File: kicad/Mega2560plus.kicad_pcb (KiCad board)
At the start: 4 copper layers, 53.3 x 101.6 mm, 146 parts, among them J1 USB_C_Receptacle_USB2.0_14P, J10 TC2030, J11 Conn_02x18_Odd_Even, J12 Conn_01x10, J13 Conn_01x08, J14 Conn_01x08, J15 Conn_02x06_Counter_Clockwise, J2 USB_C_Receptacle_USB2.0_14P, J3 Micro_SD_Card_Det2, J4 2.1mm ID 5.5mm OD PJ-102AH, J5 Conn_01x04_MountingPin, J6 Conn_01x04_MountingPin, J7 Conn_01x08, J8 Conn_01x08, J9 Conn_01x08, Q1 DMP3013SFV, SW1 SW_SPST, SW2 SW_SPST, SW3 SW_SPST, U1 USBLC6-2SC6, U10 TLV75733PDBV, U11 TLV75733PDBV, U12 SCD41-D-R2, U13 BME680, U14 LSM6DSL, U15 DS3231M, U16 SN74LVC1T45DBV, U17 SN74LVC1T45DBV, U2 FT231XS, U3 USBLC6-2SC6, U4 ESP32-S3-WROOM-1U-N16R8, U5 USBLC6-4SC6, U6 W25Q128JVS, U7 ATmega2560-16A, U8 FM24C64C, U9 TPS62163DSG

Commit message: finish pcb
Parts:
- removed the R7 at (303.0, 143.8)
- removed the R8 at (303.0, 146.3)
- added G***: LOGO, logo:empire_mask, F.Cu at (100.0, 100.0)
- added G***: LOGO, logo:linuxpenguin_cu, F.Cu at (117.8, 119.5)
- added G***: LOGO, logo:empire_cu, F.Cu at (100.0, 100.0)
- added G***: LOGO, logo:linuxpenguin-mask, F.Cu at (117.8, 119.5)
- added Y1: 16MHz X322516MLB4SI, Crystal:Crystal_SMD_3225-4Pin_3.2x2.5mm, F.Cu at (84.4, 96.2)
- BT1: footprint Battery:BatteryHolder_Keystone_1060_1x2032 -> Battery:BatteryHolder_LINX_BAT-HLD-012-SMT; moved to B.Cu
- C1, C10, C14, C15, C16, C2, C28, C29, C3, C30, C31, C32, C36, C37, C4, C5, C6, C7, C8: footprint Capacitor_SMD:C_0603_1608Metric -> Capacitor_SMD:C_0402_1005Metric
- C11: renamed from C12; value 16pF -> 18pF; footprint Capacitor_SMD:C_0603_1608Metric -> Capacitor_SMD:C_0402_1005Metric
- C12: renamed from C13; value 16pF -> 18pF; footprint Capacitor_SMD:C_0603_1608Metric -> Capacitor_SMD:C_0402_1005Metric
- C13: renamed from C11; footprint Capacitor_SMD:C_0603_1608Metric -> Capacitor_SMD:C_0402_1005Metric
- C43, C44, C45, C46, C9: footprint Capacitor_SMD:C_0603_1608Metric -> Capacitor_SMD:C_0805_2012Metric; moved to B.Cu
- D10, D11, D12, D14, D15, D16, D18, D6, D7, D8: footprint LED_SMD:LED_Avago_PLCC4_3.2x2.8mm_CW -> LED_SMD:LED_0402_1005Metric
- D2, F2, JP1, U16, U17, U5: moved to B.Cu
- J2: value USB_C_Receptacle_USB2.0_14P -> Conn_02x02_Counter_Clockwise; footprint Connector_USB:USB_C_Receptacle_HRO_TYPE-C-31-M-12 -> Connector_PinSocket_2.54mm:PinSocket_2x02_P2.54mm_Vertical
- J5, J6: footprint Connector_JST:JST_SH_SM04B-SRSS-TB_1x04-1MP_P1.00mm_Horizontal -> Connector_JST:JST_SH_BM04B-SRSS-TB_1x04-1MP_P1.00mm_Vertical
- R1, R2, R3, R4, R5: footprint Resistor_SMD:R_0603_1608Metric -> Resistor_SMD:R_0402_1005Metric
- R14: renamed from R16; footprint Resistor_SMD:R_0603_1608Metric -> Resistor_SMD:R_0805_2012Metric; moved to B.Cu
- R18: renamed from R20; footprint Resistor_SMD:R_0603_1608Metric -> Resistor_SMD:R_0402_1005Metric
- R20: renamed from R22; footprint Resistor_SMD:R_0603_1608Metric -> Resistor_SMD:R_0402_1005Metric
- R22: renamed from R24; footprint Resistor_SMD:R_0603_1608Metric -> Resistor_SMD:R_0402_1005Metric
- R23: renamed from R25; footprint Resistor_SMD:R_0603_1608Metric -> Resistor_SMD:R_0402_1005Metric
- R24: renamed from R26; footprint Resistor_SMD:R_0603_1608Metric -> Resistor_SMD:R_0402_1005Metric
- R25: renamed from R27; footprint Resistor_SMD:R_0603_1608Metric -> Resistor_SMD:R_0402_1005Metric
- R26: renamed from R28; footprint Resistor_SMD:R_0603_1608Metric -> Resistor_SMD:R_0402_1005Metric
- R27: renamed from R29; footprint Resistor_SMD:R_0603_1608Metric -> Resistor_SMD:R_0402_1005Metric
- R28: renamed from R30; footprint Resistor_SMD:R_0603_1608Metric -> Resistor_SMD:R_0402_1005Metric
- R29: renamed from R31; footprint Resistor_SMD:R_0603_1608Metric -> Resistor_SMD:R_0402_1005Metric
- R30: renamed from R32; footprint Resistor_SMD:R_0603_1608Metric -> Resistor_SMD:R_0402_1005Metric
- R31: renamed from R33; footprint Resistor_SMD:R_0603_1608Metric -> Resistor_SMD:R_0402_1005Metric
- R6: value 5.1k -> 22; footprint Resistor_SMD:R_0603_1608Metric -> Resistor_SMD:R_0402_1005Metric
- R7: renamed from R9; footprint Resistor_SMD:R_0603_1608Metric -> Resistor_SMD:R_0402_1005Metric
- R8: renamed from R10; footprint Resistor_SMD:R_0603_1608Metric -> Resistor_SMD:R_0402_1005Metric
- R9: renamed from R11; footprint Resistor_SMD:R_0603_1608Metric -> Resistor_SMD:R_0402_1005Metric
- SW2, SW3: footprint Button_Switch_SMD:SW_SPST_PTS645Sx43SMTR92 -> Button_Switch_SMD:SW_SPST_TS-1088-xR020
- moved C46 249.6 mm to (81.3, 85.3), turned to -90 degrees
- moved C32 242.9 mm to (93.4, 73.4), turned to 180 degrees
- moved C45 242.3 mm to (88.3, 85.3), turned to -90 degrees
- moved C31 240.6 mm to (93.4, 78.8), turned to 180 degrees
- moved C8 235.6 mm to (79.4, 66.0), turned to 90 degrees
- moved C29 234.9 mm to (98.2, 77.9), turned to 90 degrees
- moved R20 233.9 mm to (101.2, 80.9)
- moved C7 233.7 mm to (80.5, 66.0), turned to 90 degrees
- moved C12 233.6 mm to (84.4, 93.2), turned to 180 degrees
- moved R7 232.2 mm to (86.1, 66.1)
- moved C11 232.0 mm to (84.4, 99.2)
- moved R14 230.8 mm to (92.4, 63.9)
- moved C30 229.8 mm to (104.2, 77.9), turned to 90 degrees
- moved C15 229.6 mm to (88.9, 96.6), turned to -90 degrees
- moved R6 229.2 mm to (86.1, 67.3)
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- renumbered R12 to R10, R13 to R11, R14 to R12, R15 to R13, R17 to R15, R18 to R16, R19 to R17, R21 to R19, R23 to R21
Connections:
- C3 pad 2: UART3.3V -> +5V
- F2 pad 1: Net-(F2-Pad1) -> Net-(J2-Pin_1)
- R6 pad 1: Net-(J2-CC2) -> Net-(R6-Pad1)
- R6 pad 2: GND -> ESP32_USB_D+
- U2 pad 3: UART3.3V -> +5V
- U3 pad 1: Net-(J2-D--PadA7) -> Net-(J2-Pin_4)
- U3 pad 3: Net-(J2-D+-PadA6) -> Net-(J2-Pin_3)
- U3 pad 4: Net-(R7-Pad1) (its old number) -> Net-(R6-Pad1)
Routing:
- net GND: track 0.00 -> 242.1 mm, vias 0 -> 48
- net +3.3VP: track 0.00 -> 223.6 mm, vias 0 -> 7
- net +5V: track 0.00 -> 223.2 mm, vias 0 -> 13
- net AVR_SCL: track 0.00 -> 189.5 mm, vias 0 -> 3
- net +3.3V: track 0.00 -> 167.1 mm, vias 0 -> 12
- net AVR_SDA: track 0.00 -> 161.2 mm, vias 0 -> 3
- net /ESP32/I2C1_SCL: track 0.00 -> 154.5 mm, vias 0 -> 8
- net /ESP32/I2C1_SDA: track 0.00 -> 152.5 mm, vias 0 -> 8
- net /ESP32/RTC_INT: track 0.00 -> 92.1 mm, vias 0 -> 2
- net AVR_RESET: track 0.00 -> 80.4 mm, vias 0 -> 4
- net PB1: track 0.00 -> 75.6 mm, vias 0 -> 3
- net PB2: track 0.00 -> 74.7 mm, vias 0 -> 2
- net PB0: track 0.00 -> 73.7 mm, vias 0 -> 1
- net PB3: track 0.00 -> 73.5 mm, vias 0 -> 2
- net ESP_RESET: track 0.00 -> 70.5 mm, vias 0 -> 3
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- added copper zone on In2.Cu, net +3.3V
- added copper zone on In2.Cu, net +3.3VP
- added copper zone on In2.Cu, net +5V
- added copper zone on In4.Cu, net GND
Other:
- copper layers 4 -> 6
- board text added: "3.3V"
- board text added: "5V"
- board text added: "Converts Bitcoins into Dreams."
- board text added: "Designed in Canada"
- board text added: "Keep Going!"
- board text added: "Mega 2560+"

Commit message: add spinning render
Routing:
- net ESP32_NPX: track 0.00 -> 63.3 mm, vias 0 -> 2
- net AVR_SDA: track 161.2 -> 144.5 mm, vias 3 -> 2
- net AVR_SCL: track 189.5 -> 173.0 mm, vias 3 -> 2
- net +5V: track 223.2 -> 227.2 mm, vias 13 -> 14
- net Net-(D18-A): track 0.00 -> 1.01 mm
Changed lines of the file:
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@@
 	)
 	(segment
+		(start 116.395 82.905)
+		(end 116.8 82.5)
+		(width 0.2)
+		(layer "F.Cu")
+		(net "+5V")
+	)
+	(segment
 		(start 107.9 65.49)
 		(end 107.385 65.49)
@@
 	)
 	(segment
+		(start 116.395 84.325)
+		(end 116.395 82.905)
+		(width 0.2)
+		(layer "F.Cu")
+		(net "+5V")
+	)
+	(segment
 		(start 82.275 87.475001)
 		(end 82.1 87.650001)
@@
 	)
 	(via
+		(at 116.8 82.5)
+		(size 0.6)
+		(drill 0.3)
+		(layers "F.Cu" "B.Cu")
+		(net "+5V")
+	)
+	(via
 		(at 117.925 128.3)
 		(size 0.6)
@@
 	)
 	(segment
+		(start 117 83.55)
+		(end 117.65 84.2)
+		(width 0.2)
+		(layer "B.Cu")
+		(net "+5V")
+	)
+	(segment
 		(start 109.525 84.625)
 		(end 109.525 83.1)
@@
 	)
 	(segment
+		(start 116.8 82.5)
+		(end 117 82.7)
+		(width 0.2)
+		(layer "B.Cu")
+		(net "+5V")
+	)
+	(segment
 		(start 88.35 84.35)
 		(end 85.9875 84.35)
@@
 	)
 	(segment
+		(start 117 82.7)
+		(end 117 83.55)
+		(width 0.2)
+		(layer "B.Cu")
+		(net "+5V")
+	)
+	(segment
 		(start 114.315552 84.2)
 		(end 113.365552 85.15)
@@
 	)
 	(segment
-		(start 93.1 71.9)
-		(end 94.1 71.9)
+		(start 91.6 77.65)
+		(end 91.6 72.7)
 		(width 0.2)
 		(layer "In3.Cu")
@@
 	)
 	(segment
-		(start 92.3 72.7)
-		(end 93.1 71.9)
+		(start 91.6 72.7)
+		(end 93.3 71)
 		(width 0.2)
 		(layer "In3.Cu")
@@
 	)
 	(segment
-		(start 92.3 76.95)
-		(end 92.3 72.7)
+		(start 93.3 71)
+		(end 95 71)
 		(width 0.2)
 		(layer "In3.Cu")
@@
 	)
 	(segment
-		(start 94.1 71.9)
+		(start 95 71)
 		(end 103.79 62.21)
 		(width 0.2)
@@
 	(segment
 		(start 84 85.25)
-		(end 92.3 76.95)
+		(end 91.6 77.65)
 		(width 0.2)
 		(layer "In3.Cu")
 		(net "/ESP32/RTC_INT")
 	)
+	(segment
+		(start 107.3 61.54)
+		(end 106.7 60.94)
+		(width 0.2)
+		(layer "F.Cu")
+		(net "ESP32_NPX")
+	)
+	(segment
+		(start 90.95 109.82)
+		(end 93.395 107.375)
+		(width 0.2)
+		(layer "F.Cu")
+		(net "ESP32_NPX")
+	)
+	(segment
+		(start 93.395 90.095)
+		(end 91 87.7)
+		(width 0.2)
+		(layer "F.Cu")
+		(net "ESP32_NPX")
+	)
+	(segment
+		(start 106.7 60.94)
+		(end 105.75 60.94)
+		(width 0.2)
+		(layer "F.Cu")
+		(net "ESP32_NPX")
+	)
+	(segment
+		(start 94.751471 98.297058)
+		(end 94.751471 96.6)
+		(width 0.2)
+		(layer "F.Cu")
+		(net "ESP32_NPX")
+	)
+	(segment
+		(start 93.395 99.653529)
+		(end 94.751471 98.297058)
+		(width 0.2)
+		(layer "F.Cu")
+		(net "ESP32_NPX")
+	)
+	(segment
+		(start 93.395 95.243529)
+		(end 93.395 90.095)
+		(width 0.2)
+		(layer "F.Cu")
+		(net "ESP32_NPX")
+	)
+	(segment
+		(start 94.751471 96.6)
+		(end 93.395 95.243529)
+		(width 0.2)
+		(layer "F.Cu")
+		(net "ESP32_NPX")
+	)
+	(segment
+		(start 107.3 63.9)
+		(end 107.3 61.54)
+		(width 0.2)
+		(layer "F.Cu")
+		(net "ESP32_NPX")
+	)
+	(segment
+		(start 93.395 107.375)
+		(end 93.395 99.653529)
+		(width 0.2)
+		(layer "F.Cu")
+		(net "ESP32_NPX")
+	)
+	(via
+		(at 107.3 63.9)
+		(size 0.6)
+		(drill 0.3)
+		(layers "F.Cu" "B.Cu")
+		(net "ESP32_NPX")
+	)
+	(via
+		(at 91 87.7)
+		(size 0.6)
+		(drill 0.3)
+		(layers "F.Cu" "B.Cu")
+		(net "ESP32_NPX")
+	)
+	(segment
+		(start 92 73.471471)
+		(end 94.071471 71.4)
+		(width 0.2)
+		(layer "In3.Cu")
+		(net "ESP32_NPX")
+	)
+	(segment
+		(start 94.071471 71.4)
+		(end 95.165686 71.4)
+		(width 0.2)
+		(layer "In3.Cu")
+		(net "ESP32_NPX")
+	)
+	(segment
+		(start 91 87.7)
+		(end 92 86.7)
+		(width 0.2)
+		(layer "In3.Cu")
+		(net "ESP32_NPX")
+	)
+	(segment
+		(start 95.165686 71.4)
+		(end 102.665686 63.9)
+		(width 0.2)
+		(layer "In3.Cu")
+		(net "ESP32_NPX")
+	)
+	(segment
+		(start 102.665686 63.9)
+		(end 107.3 63.9)
+		(width 0.2)
+		(layer "In3.Cu")
+		(net "ESP32_NPX")
+	)
+	(segment
+		(start 92 86.7)
+		(end 92 73.471471)
+		(width 0.2)
+		(layer "In3.Cu")
+		(net "ESP32_NPX")
+	)
 	(via
 		(at 105.75 59.67)
@@
 	)
 	(segment
+		(start 79.585 111.2)
+		(end 80.59 111.2)
+		(width 0.2)
+		(layer "F.Cu")
+		(net "Net-(D18-A)")
+	)
+	(segment
 		(start 120.825 129.425001)
 		(end 120.825 133)
@@
 	)
 	(via
-		(at 106.1 79.7)
-		(size 0.6)
-		(drill 0.3)
-		(layers "F.Cu" "B.Cu")
-		(net "AVR_SDA")
-	)
-	(via
 		(at 87 104.995)
 		(size 0.6)
@@
 	)
 	(segment
-		(start 106.1 80.3)
-		(end 106.1 79.7)
-		(width 0.2)
-		(layer "In2.Cu")
-		(net "AVR_SDA")
-	)
-	(segment
-		(start 109.090686 83.925)
-		(end 106.775735 81.610049)
-		(width 0.2)
-		(layer "In2.Cu")
-		(net "AVR_SDA")
-	)
-	(segment
-		(start 120.205 84.325)
-		(end 119.805 83.925)
-		(width 0.2)
-		(layer "In2.Cu")
-		(net "AVR_SDA")
-	)
-	(segment
-		(start 106.775735 81.610049)
-		(end 106.775735 80.975735)
-		(width 0.2)
-		(layer "In2.Cu")
-		(net "AVR_SDA")
-	)
-	(segment
 		(start 104.365686 134.1)
 		(end 85.4 115.134314)
@@
 	)
 	(segment
-		(start 106.775735 80.975735)
-		(end 106.1 80.3)
-		(width 0.2)
-		(layer "In2.Cu")
-		(net "AVR_SDA")
-	)
-	(segment
 		(start 85.4 115.134314)
 		(end 85.4 106.595)
@@
 	)
 	(segment
-		(start 119.805 83.925)
-		(end 109.090686 83.925)
-		(width 0.2)
-		(layer "In2.Cu")
-		(net "AVR_SDA")
-	)
-	(segment
 		(start 118.935 85.365)
 		(end 118.9 85.4)
@@
 		(net "AVR_SCL")
 	)
-	(via
-		(at 105.3 79.7)
-		(size 0.6)
-		(drill 0.3)
-		(layers "F.Cu" "B.Cu")
-		(net "AVR_SCL")
-	)
 	(segment
 		(start 124.15 68)
@@
 	)
 	(segment
-		(start 117.825 84.325)
-		(end 108.925 84.325)
-		(width 0.2)
-		(layer "In2.Cu")
-		(net "AVR_SCL")
-	)
-	(segment
-		(start 108.925 84.325)
-		(end 105.3 80.7)
-		(width 0.2)
-		(layer "In2.Cu")
-		(net "AVR_SCL")
-	)
-	(segment
 		(start 123.095 134.5)
 		(end 124.15 135.555)
@@
 	)
 	(segment
-		(start 118.9 85.4)
-		(end 117.825 84.325)
-		(width 0.2)
-		(layer "In2.Cu")
-		(net "AVR_SCL")
-	)
-	(segment
 		(start 85 115.3)
 		(end 104.2 134.5)
 		(width 0.2)
 		(layer "In2.Cu")
-		(net "AVR_SCL")
-	)
-	(segment
-		(start 105.3 80.7)
-		(end 105.3 79.7)
-		(width 0.2)
-		(layer "In2.Cu")

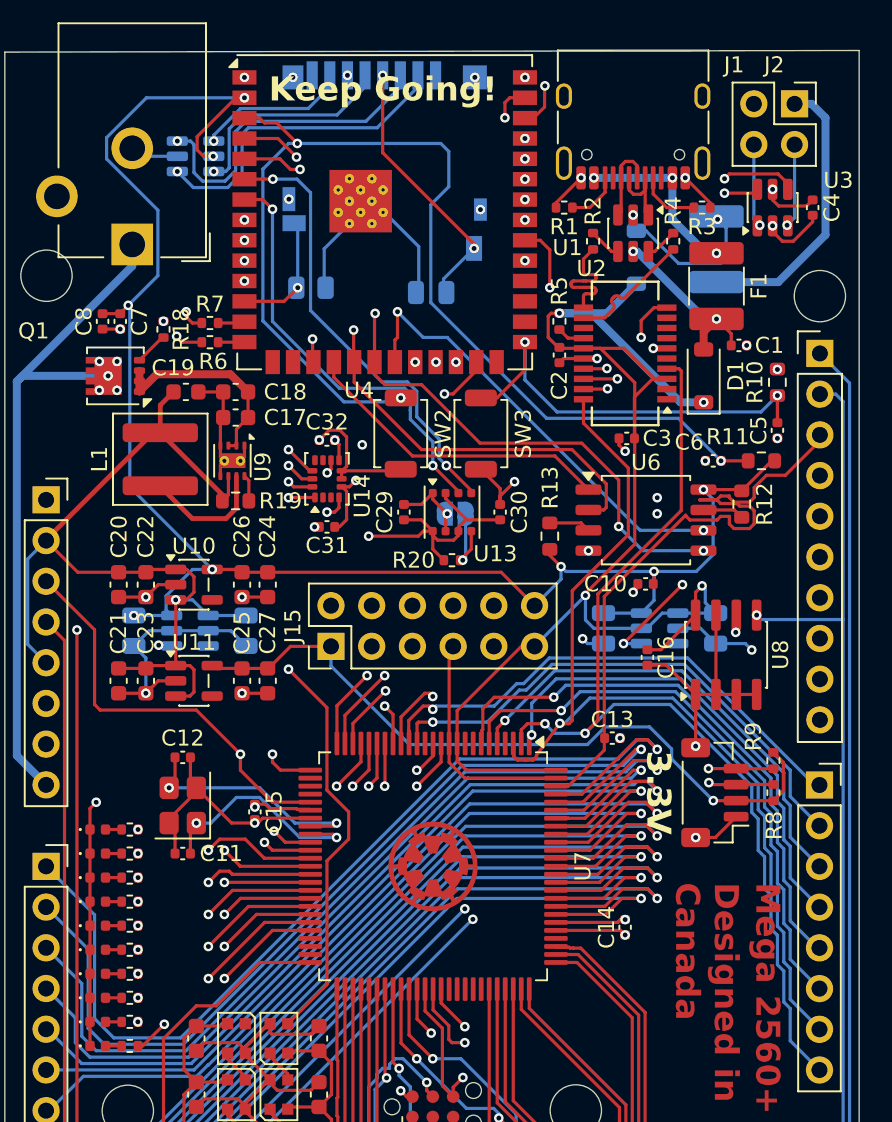
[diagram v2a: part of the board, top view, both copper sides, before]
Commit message: fix silkscreen
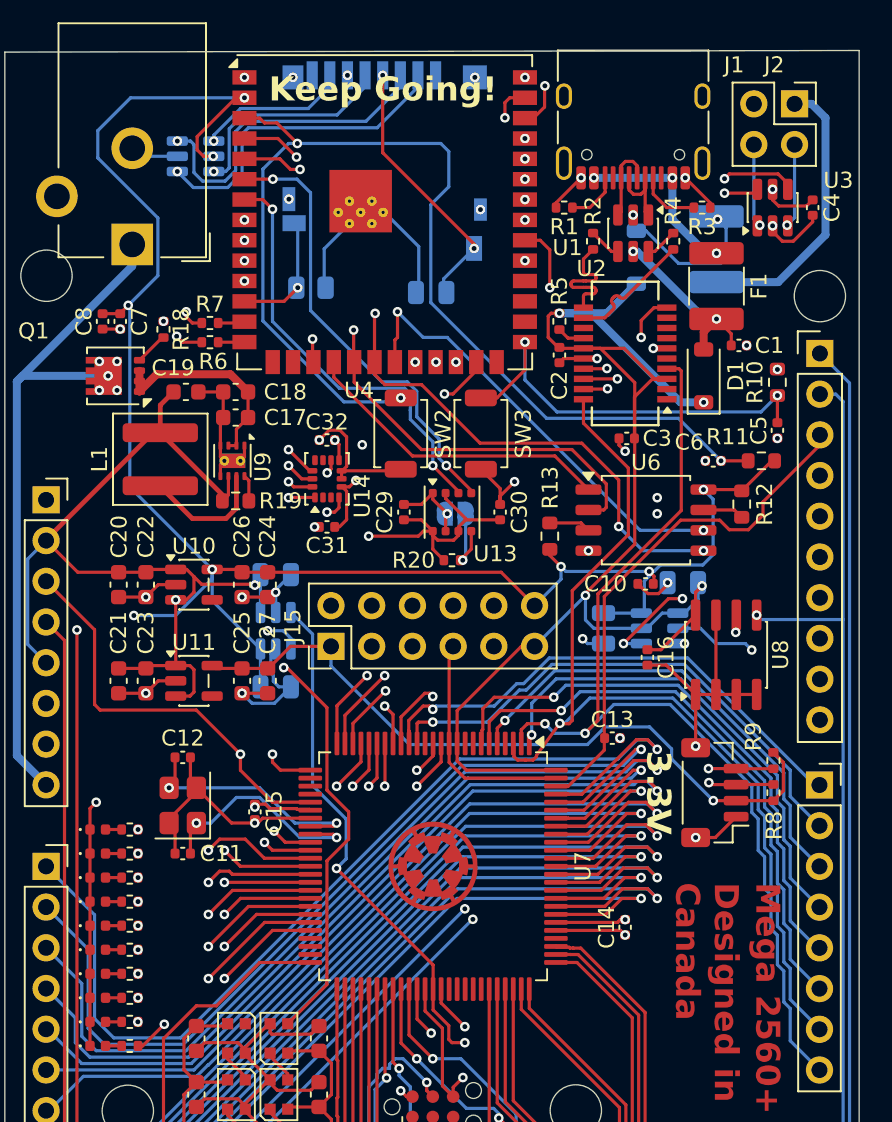
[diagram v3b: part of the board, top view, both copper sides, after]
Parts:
- moved C46 9.52 mm to (90.2, 88.8), turned to 0 degrees
- moved U17 5.35 mm to (90.2, 85.3), turned to -90 degrees
- moved C45 3.96 mm to (90.2, 81.8), turned to 0 degrees
- moved C43 3.51 mm to (115.6, 82.3), turned to 180 degrees
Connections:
- U16 pad 3: ATMEGA_TX -> AVR_TX3
- U17 pad 3: ATMEGA_RX -> AVR_RX3
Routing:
- net AVR_TX3: track 28.3 -> 63.9 mm, vias 1 -> 2
- net AVR_RX3: track 30.6 -> 58.3 mm, vias 1 -> 2
- net +5V: track 227.2 -> 240.5 mm, vias 14 -> 15
- net +3.3V: track 167.1 -> 175.8 mm
- net AREF: track 40.5 -> 32.5 mm
- net /ESP32/UART1_TX: track 40.4 -> 38.9 mm
- net GND: track 242.1 -> 242.8 mm, vias 48 -> 49
- net ESP32_NPX: track 63.3 -> 63.9 mm
- net /ESP32/UART1_RX: track 57.0 -> 57.5 mm
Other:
- board text added: "22 24 26 28 30 32 34 36 38 40 42 44 46 48 50 52"
- board text added: "31 33 35 37 39 41 43 45 47 49 51 53"
- board text added: "A0 A1 A2 A3 A4 A5 6 A7"
- board text added: "A8 A9 A10 A11 A12 A13 A14 A15"
- board text added: "D7 D6 D5 D4 D3 D2 TX0 -> D1 RX0 <- D0"
- board text added: "IOREF RESET 3.3V 5V GND GND Vin"
- board text added: "SCL SDA AREF GND D13 D12 D11 D10 D9 D8"
- board text added: "TX3 D14 RX3 D15 TX2 D16 RX2 D17 TX1 D18 RX1 D19 SDA D20 SCL D21"
